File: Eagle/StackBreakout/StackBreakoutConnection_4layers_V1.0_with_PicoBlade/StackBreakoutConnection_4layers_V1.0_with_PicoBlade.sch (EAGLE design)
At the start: 9 parts, among them J1 SSQ-126-23-G-D, J2 SSQ-126-23-G-D

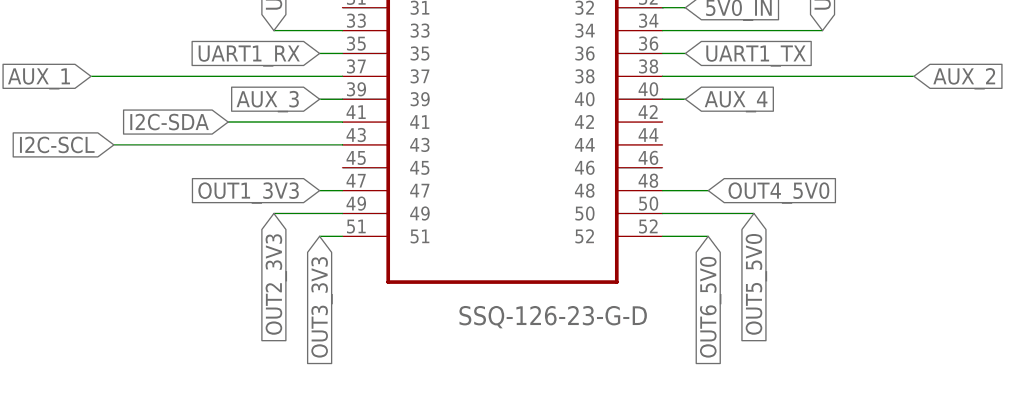
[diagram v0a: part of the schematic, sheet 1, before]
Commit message: Output voltage pin update
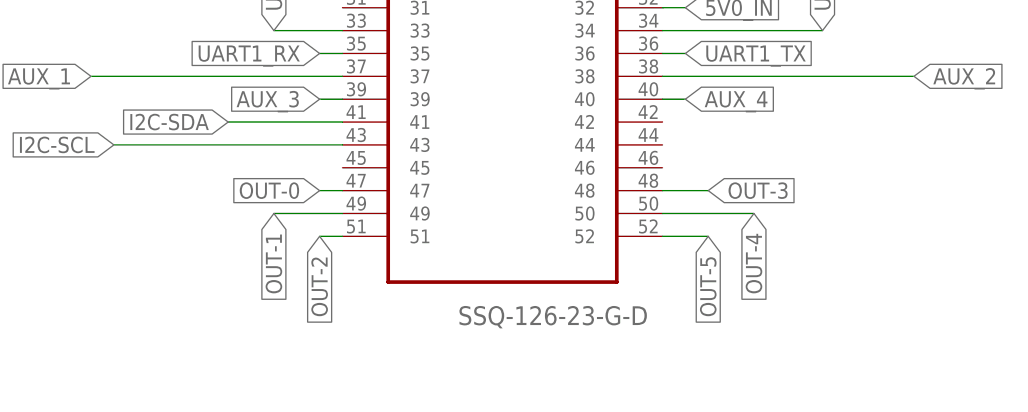
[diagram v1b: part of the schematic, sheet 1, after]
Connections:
- net OUT1_3V3 renamed OUT-0
- net OUT2_3V3 renamed OUT-1
- net OUT3_3V3 renamed OUT-2
- net OUT4_5V0 renamed OUT-3
- net OUT5_5V0 renamed OUT-4
- net OUT6_5V0 renamed OUT-5

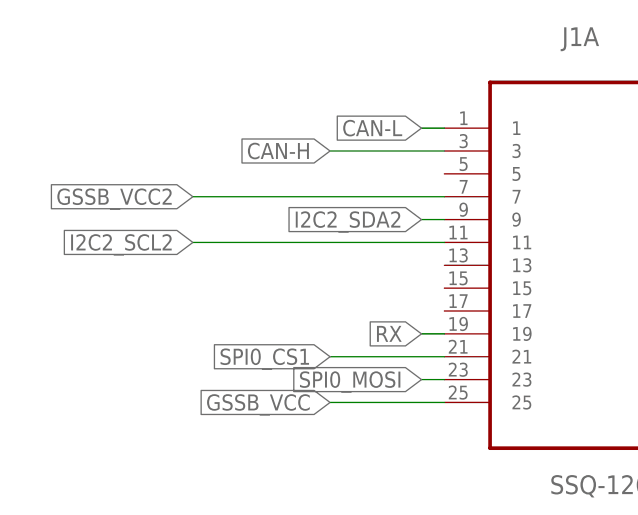
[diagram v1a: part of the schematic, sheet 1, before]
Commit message: update i2c pinout
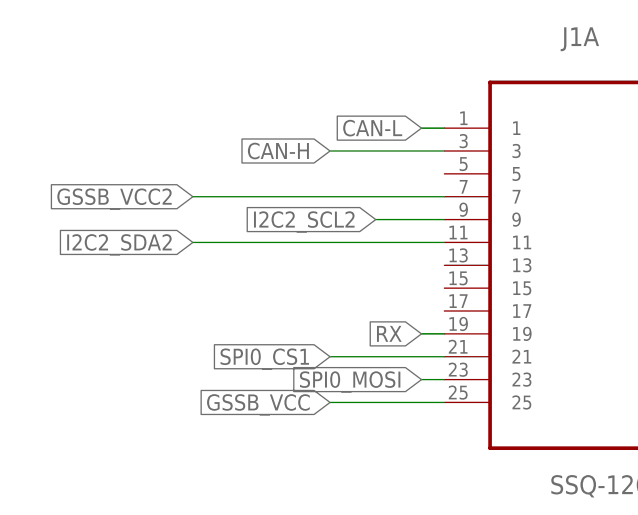
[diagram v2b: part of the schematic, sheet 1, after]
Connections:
- net I2C2_SCL2: now also J1A.9; no longer J1A.11
- net I2C2_SDA2: now also J1A.11; no longer J1A.9
